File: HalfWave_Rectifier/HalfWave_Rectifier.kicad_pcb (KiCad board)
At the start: 2 copper layers, 47 x 13.5 mm, 4 parts, among them J1 Screw_Terminal_01x02, J2 Screw_Terminal_01x02

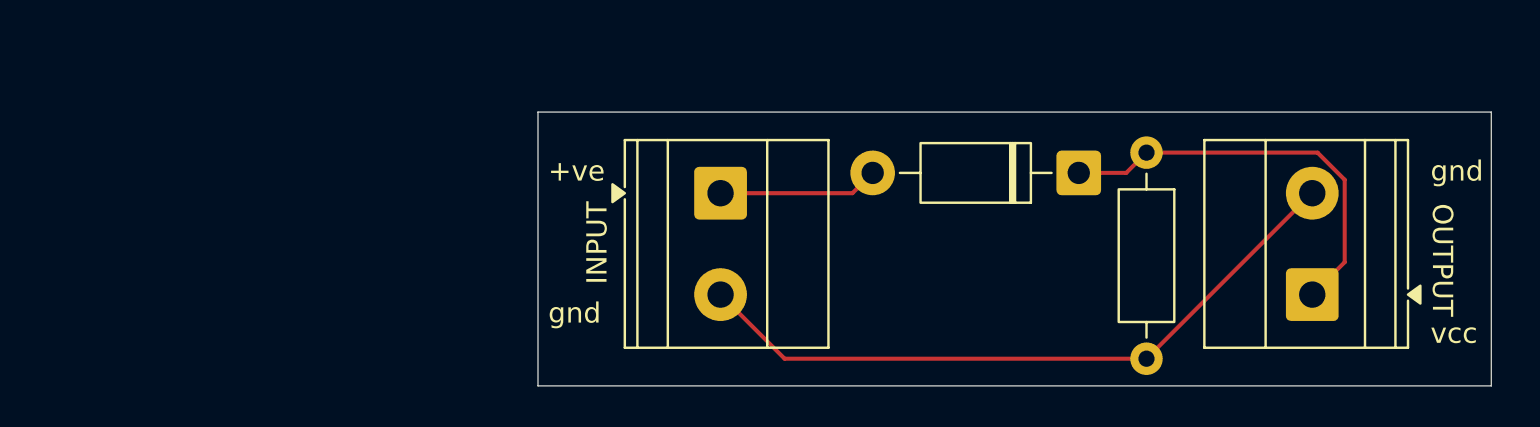
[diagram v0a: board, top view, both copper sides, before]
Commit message: Halfwave Modified with transformer
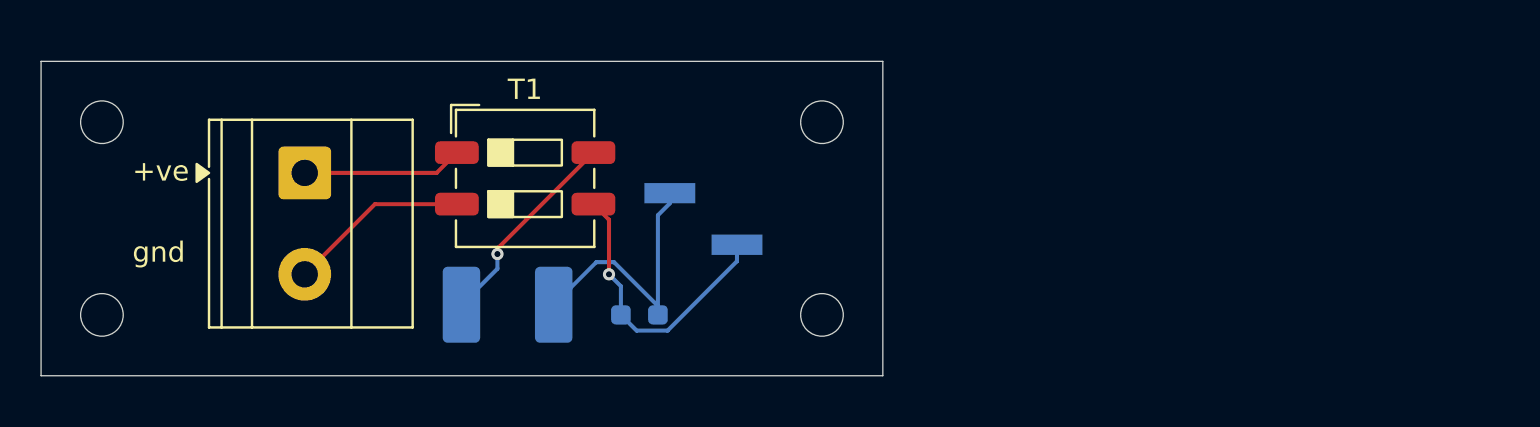
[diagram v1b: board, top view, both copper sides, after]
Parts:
- added H1: MountingHole, MountingHole:MountingHole_2.1mm, F.Cu at (88.0, 78.0)
- added H2: MountingHole, MountingHole:MountingHole_2.1mm, F.Cu at (88.0, 87.5)
- added H3: MountingHole, MountingHole:MountingHole_2.1mm, F.Cu at (123.5, 78.0)
- added H4: MountingHole, MountingHole:MountingHole_2.1mm, F.Cu at (123.5, 87.5)
- added T1: Transformer_1P_1S, Button_Switch_SMD:SW_DIP_SPSTx02_Slide_6.7x6.64mm_W6.73mm_P2.54mm_LowProfile_JPin, F.Cu at (108.9, 80.8)
- D1: footprint Diode_THT:D_DO-41_SOD81_P10.16mm_Horizontal -> Diode_SMD:D_2114_3652Metric_Pad1.85x3.75mm_HandSolder; moved to B.Cu
- J2: value Screw_Terminal_01x02 -> Conn_01x02_Pin; footprint TerminalBlock_Phoenix:TerminalBlock_Phoenix_MKDS-1,5-2_1x02_P5.00mm_Horizontal -> Connector_PinHeader_2.54mm:PinHeader_1x02_P2.54mm_Vertical_SMD_Pin1Right; moved to B.Cu
- R1: footprint Resistor_THT:R_Axial_DIN0207_L6.3mm_D2.5mm_P10.16mm_Horizontal -> Resistor_SMD:R_0603_1608Metric_Pad0.98x0.95mm_HandSolder; moved to B.Cu
- moved J2 30.2 mm to (117.7, 82.8), turned to 0 degrees
- moved D1 28.9 mm to (108.0, 87.0)
- moved R1 26.2 mm to (114.5, 87.5), turned to 180 degrees
- moved J1 20.5 mm to (98.0, 80.5)
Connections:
- J1 pad 1: Net-(D1-A) -> Net-(J1-Pin_1)
- J1 pad 2: GND -> Net-(J1-Pin_2)
- J2 pad 1: Net-(D1-K) -> GND
- J2 pad 2: GND -> Net-(D1-K)
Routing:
- net GND: track 33.9 -> 14.3 mm, vias 0 -> 1
- net Net-(J1-Pin_2): track 0.00 -> 8.93 mm
- net Net-(J1-Pin_1): track 0.00 -> 7.91 mm
- net Net-(D1-K): track 20.4 -> 13.6 mm
- net Net-(D1-A): track 7.91 -> 10.2 mm, vias 0 -> 1
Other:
- board size 47 x 13.5 mm -> 41.5 x 15.5 mm
- board text removed: "INPUT"
- board text removed: "OUTPUT"
- board text removed: "vcc"

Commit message: Correct Footprint of transformer and reduced hole size
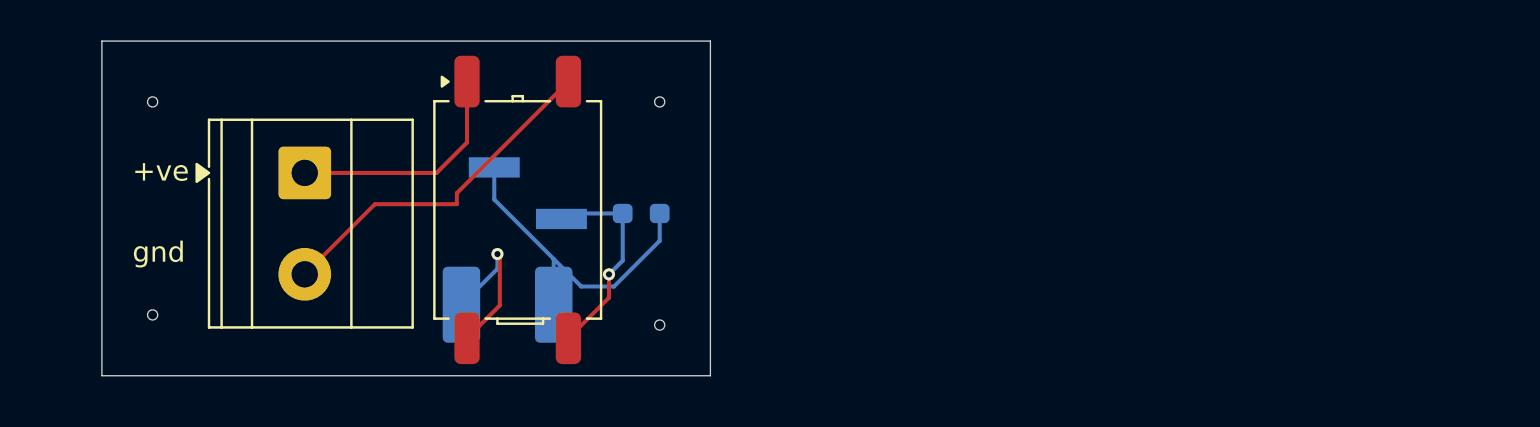
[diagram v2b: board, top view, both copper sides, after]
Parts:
- T1: footprint Button_Switch_SMD:SW_DIP_SPSTx02_Slide_6.7x6.64mm_W6.73mm_P2.54mm_LowProfile_JPin -> Transformer_SMD:Transformer_ED8_4-Lead_10.5x8mm_P5mm
- moved J2 8.75 mm to (109.0, 81.5)
- moved H3 8.06 mm to (115.5, 77.0)
- moved H4 8.02 mm to (115.5, 88.0)
- moved R1 5.00 mm to (114.6, 82.5)
- moved H1 2.69 mm to (90.5, 77.0)
- moved H2 2.50 mm to (90.5, 87.5)
- moved T1 1.60 mm to (108.5, 82.3)
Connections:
- net GND renamed Net-(J2-Pin_1)
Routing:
- net Net-(J1-Pin_2): track 8.93 -> 17.3 mm
- net Net-(J2-Pin_1): track 14.3 -> 10.4 mm
- net Net-(J1-Pin_1): track 7.91 -> 11.6 mm
- net Net-(D1-K): track 13.6 -> 16.4 mm
- net Net-(D1-A): track 10.2 -> 8.10 mm
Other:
- board size 41.5 x 15.5 mm -> 30 x 16.5 mm
